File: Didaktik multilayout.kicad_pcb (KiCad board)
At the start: 2 copper layers, 212.7 x 79.4 mm, 121 parts, among them J1 Conn_01x04_MountingPin, J2 AVR-ISP-6, SW1 SW_Push_45deg, SW10 SW_Push_45deg, SW11 SW_Push_45deg, SW12 SW_Push_45deg, SW13 SW_Push_45deg, SW14 SW_Push_45deg, SW15 SW_Push_45deg, SW16 SW_Push_45deg, SW17 SW_Push_45deg, SW18 SW_Push_45deg, SW19 SW_Push_45deg, SW2 SW_Push_45deg, SW20 SW_Push_45deg, SW21 SW_Push_45deg, SW22 SW_Push_45deg, SW23 SW_Push_45deg, SW24 SW_Push_45deg, SW25 SW_Push_45deg, SW26 SW_Push_45deg, SW27 SW_Push_45deg, SW28 SW_Push_45deg, SW29 SW_Push_45deg, SW3 SW_Push_45deg, SW30 SW_Push_45deg, SW31 SW_Push_45deg, SW31a1 SW_Push_45deg, SW32 SW_Push_45deg, SW32a1 SW_Push_45deg, SW33 SW_Push_45deg, SW33a1 SW_Push_45deg, SW34 SW_Push_45deg, SW34a1 SW_Push_45deg, SW34b1 SW_Push_45deg, SW35 SW_Push_45deg, SW35a1 SW_Push_45deg, SW35b1 SW_Push_45deg, SW35c1 SW_Push_45deg, SW36 SW_Push_45deg, SW36a1 SW_Push_45deg, SW36b1 SW_Push_45deg, SW36c1 SW_Push_45deg, SW37 SW_Push_45deg, SW37a1 SW_Push_45deg, SW37b1 SW_Push_45deg, SW38 SW_Push_45deg, SW38a1 SW_Push_45deg, SW39 SW_Push_45deg, SW39a1 SW_Push_45deg, SW4 SW_Push_45deg, SW40 SW_Push_45deg, SW40a1 SW_Push_45deg, SW5 SW_Push_45deg, SW6 SW_Push_45deg, SW7 SW_Push_45deg, SW8 SW_Push_45deg, SW9 SW_Push_45deg, U1 ATmega32U4-M, Y1 Crystal_GND24_Small

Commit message: redoing placement, first routing line tests
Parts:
- moved D32 6.55 mm to (196.8, 79.4)
- moved D36 6.55 mm to (215.9, 79.4)
- moved D40 6.55 mm to (234.9, 79.4)
- moved D23 6.35 mm to (158.8, 81.0)
- moved D28 6.35 mm to (177.8, 81.0)
- moved D15 6.35 mm to (120.7, 81.0)
- moved D3 6.35 mm to (63.5, 81.0)
- moved D11 6.35 mm to (101.6, 81.0)
- moved D19 6.35 mm to (139.7, 81.0)
- moved D7 6.35 mm to (82.5, 81.0)
- moved D16 3.55 mm to (101.6, 101.6)
- moved D12 3.18 mm to (76.2, 101.6)
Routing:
- net ROW2: track 0.00 -> 58.4 mm
- net ROW3: track 0.00 -> 25.4 mm
- net Net-(D12-Pad2): track 0.00 -> 7.11 mm
- net Net-(D36-Pad2): track 0.00 -> 3.69 mm
- net Net-(D32-Pad2): track 0.00 -> 3.69 mm
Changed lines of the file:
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@@
   )
   (footprint "Diode_SMD:D_SOD-123" (layer "B.Cu")
-    (at 228.6 80.9625 90)
+    (at 234.95 79.375 90)
     (descr "SOD-123")
     (tags "SOD-123")
@@
   )
   (footprint "Diode_SMD:D_SOD-123" (layer "B.Cu")
-    (at 57.15 80.9625 90)
+    (at 63.5 80.9625 90)
     (descr "SOD-123")
     (tags "SOD-123")
@@
   )
   (footprint "Diode_SMD:D_SOD-123" (layer "B.Cu")
-    (at 209.55 80.9625 90)
+    (at 215.9 79.375 90)
     (descr "SOD-123")
     (tags "SOD-123")
@@
   )
   (footprint "Diode_SMD:D_SOD-123" (layer "B.Cu")
-    (at 190.5 80.9625 90)
+    (at 196.85 79.375 90)
     (descr "SOD-123")
     (tags "SOD-123")
@@
   )
   (footprint "Diode_SMD:D_SOD-123" (layer "B.Cu")
-    (at 114.3 80.9625 90)
+    (at 120.65 80.9625 90)
     (descr "SOD-123")
     (tags "SOD-123")
@@
   )
   (footprint "Diode_SMD:D_SOD-123" (layer "B.Cu")
-    (at 152.4 80.9625 90)
+    (at 158.75 81.025 90)
     (descr "SOD-123")
     (tags "SOD-123")
@@
   )
   (footprint "Diode_SMD:D_SOD-123" (layer "B.Cu")
-    (at 76.2 80.9625 90)
+    (at 82.55 80.9625 90)
     (descr "SOD-123")
     (tags "SOD-123")
@@
   )
   (footprint "Diode_SMD:D_SOD-123" (layer "B.Cu")
-    (at 76.2 104.775 90)
+    (at 76.2 101.6 90)
     (descr "SOD-123")
     (tags "SOD-123")
@@
   )
   (footprint "Diode_SMD:D_SOD-123" (layer "B.Cu")
-    (at 100.0125 104.775 90)
+    (at 101.6 101.6 90)
     (descr "SOD-123")
     (tags "SOD-123")
@@
   )
   (footprint "Diode_SMD:D_SOD-123" (layer "B.Cu")
-    (at 171.45 80.9625 90)
+    (at 177.8 80.9625 90)
     (descr "SOD-123")
     (tags "SOD-123")
@@
   )
   (footprint "Diode_SMD:D_SOD-123" (layer "B.Cu")
-    (at 133.35 80.9625 90)
+    (at 139.7 80.9625 90)
     (descr "SOD-123")
     (tags "SOD-123")
@@
   )
   (footprint "Diode_SMD:D_SOD-123" (layer "B.Cu")
-    (at 95.25 80.9625 90)
+    (at 101.6 80.9625 90)
     (descr "SOD-123")
     (tags "SOD-123")
@@
     (effects (font (size 1 1) (thickness 0.15)) (justify mirror))
   )
+  (segment (start 91.44 93.345) (end 91.44 100.457) (width 0.25) (layer "B.Cu") (net 12))
+  (segment (start 196.215 74.295) (end 196.85 74.93) (width 0.25) (layer "B.Cu") (net 29))
+  (segment (start 196.85 74.93) (end 196.85 77.725) (width 0.25) (layer "B.Cu") (net 29))
+  (segment (start 215.265 74.295) (end 215.9 74.93) (width 0.25) (layer "B.Cu") (net 33))
+  (segment (start 215.9 74.93) (end 215.9 77.725) (width 0.25) (layer "B.Cu") (net 33))
+  (segment (start 76.2 103.25) (end 101.6 103.25) (width 0.25) (layer "B.Cu") (net 72))
+  (segment (start 197.568901 81.743901) (end 215.181099 81.743901) (width 0.25) (layer "B.Cu") (net 73))
+  (segment (start 234.231099 81.743901) (end 234.95 81.025) (width 0.25) (layer "B.Cu") (net 73))
+  (segment (start 215.9 81.025) (end 216.618901 81.743901) (width 0.25) (layer "B.Cu") (net 73))
+  (segment (start 216.618901 81.743901) (end 234.231099 81.743901) (width 0.25) (layer "B.Cu") (net 73))
+  (segment (start 158.75 82.675) (end 177.7375 82.675) (width 0.25) (layer "B.Cu") (net 73))
+  (segment (start 215.181099 81.743901) (end 215.9 81.025) (width 0.25) (layer "B.Cu") (net 73))
+  (segment (start 196.85 81.025) (end 197.568901 81.743901) (width 0.25) (layer "B.Cu") (net 73))
+  (segment (start 177.7375 82.675) (end 177.8 82.6125) (width 0.25) (layer "B.Cu") (net 73))
   (zone (net 0) (net_name "") (layers F&B.Cu) (hatch edge 0.508)
     (connect_pads (clearance 0))

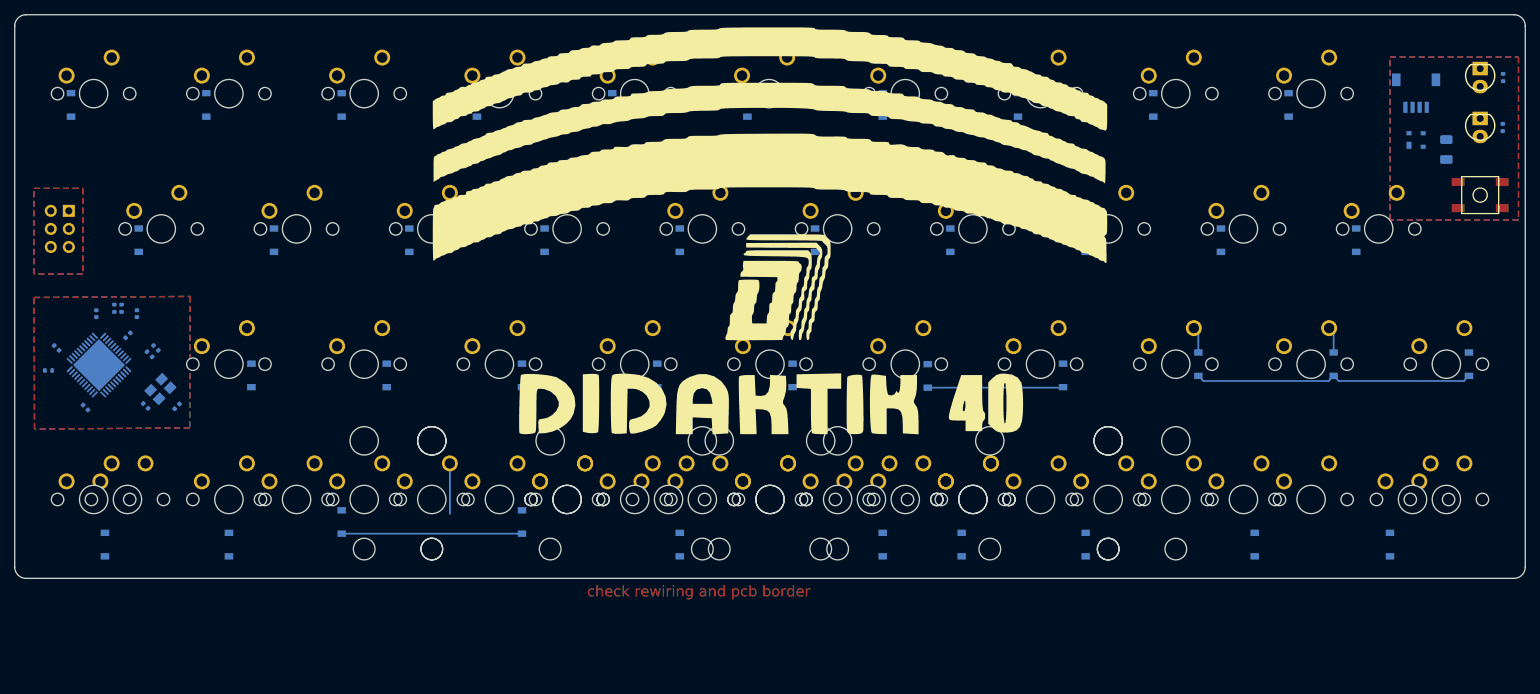
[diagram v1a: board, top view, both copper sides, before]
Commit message: revision multilayout
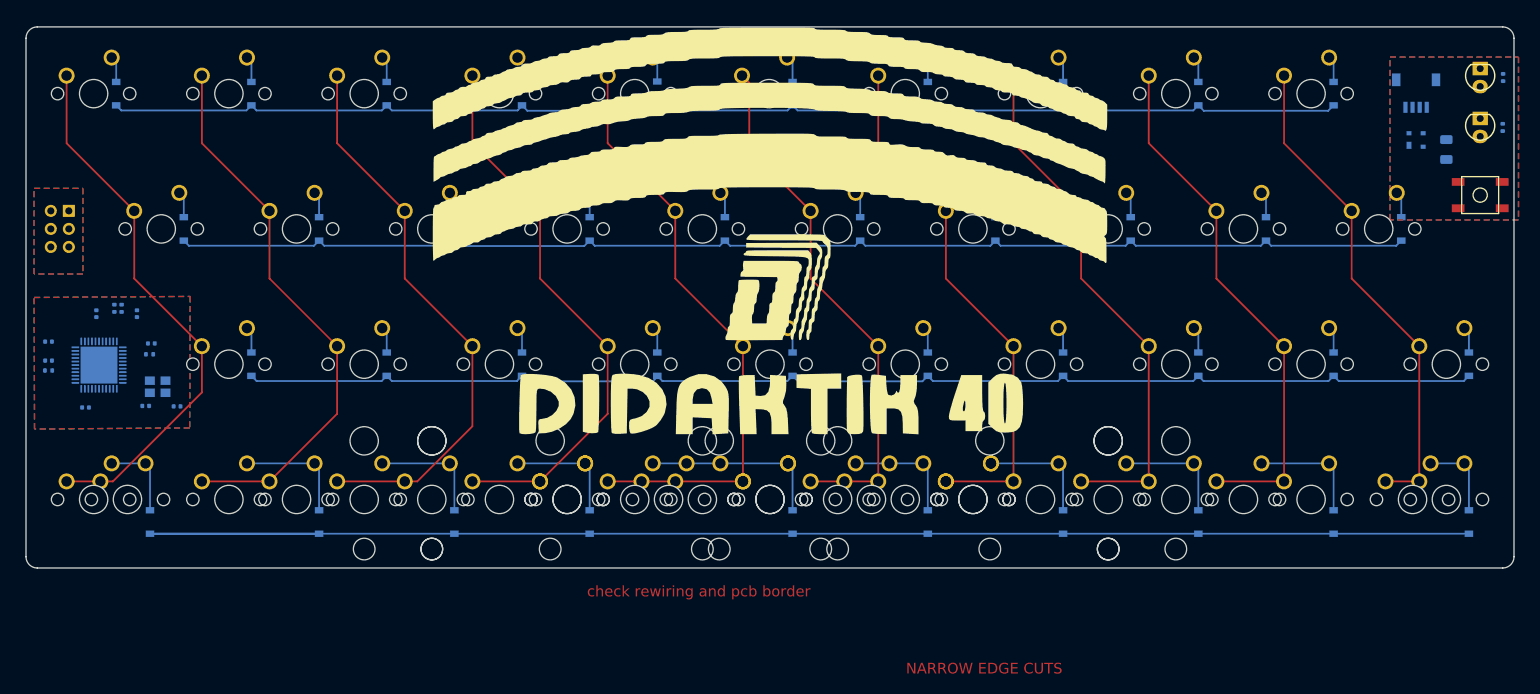
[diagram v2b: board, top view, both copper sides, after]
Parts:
- moved D33 16.2 mm to (196.8, 101.6)
- moved D20 16.2 mm to (139.7, 101.6)
- moved D12 15.9 mm to (92.1, 101.6)
- moved D29 14.6 mm to (177.8, 101.6)
- moved D8 13.1 mm to (73.0, 101.6)
- moved C6 11.7 mm to (34.9, 78.9), turned to 0 degrees
- moved D37 11.6 mm to (215.9, 101.6)
- moved D41 11.6 mm to (234.9, 101.6)
- moved D16 9.53 mm to (111.1, 101.6)
- moved D4 7.10 mm to (49.2, 101.6)
- moved D24 7.10 mm to (158.8, 101.6)
- moved D17 6.56 mm to (120.7, 41.2)
- moved D30 6.55 mm to (177.8, 41.3)
- moved D39 6.55 mm to (225.4, 60.3)
- moved D10 6.55 mm to (92.1, 60.3)
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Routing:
- net ROW3: track 25.4 -> 209.5 mm
- net ROW0: track 0.00 -> 177.0 mm
- net ROW1: track 0.00 -> 176.8 mm
- net ROW2: track 58.4 -> 177.0 mm
- net COL4: track 0.00 -> 84.1 mm
- net COL2: track 0.00 -> 79.5 mm
- net COL3: track 0.00 -> 78.5 mm
- net COL1: track 0.00 -> 78.5 mm
- net COL0: track 0.00 -> 76.8 mm
- net COL5: track 0.00 -> 74.6 mm
- net COL7: track 0.00 -> 74.6 mm
- net COL6: track 0.00 -> 74.6 mm
- net COL8: track 0.00 -> 74.6 mm
- net COL9: track 0.00 -> 69.8 mm
- net Net-(D20-Pad2): track 0.00 -> 25.9 mm
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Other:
- board size 212.7 x 79.4 mm -> 209.6 x 76.2 mm
- board text added: "NARROW EDGE CUTS"

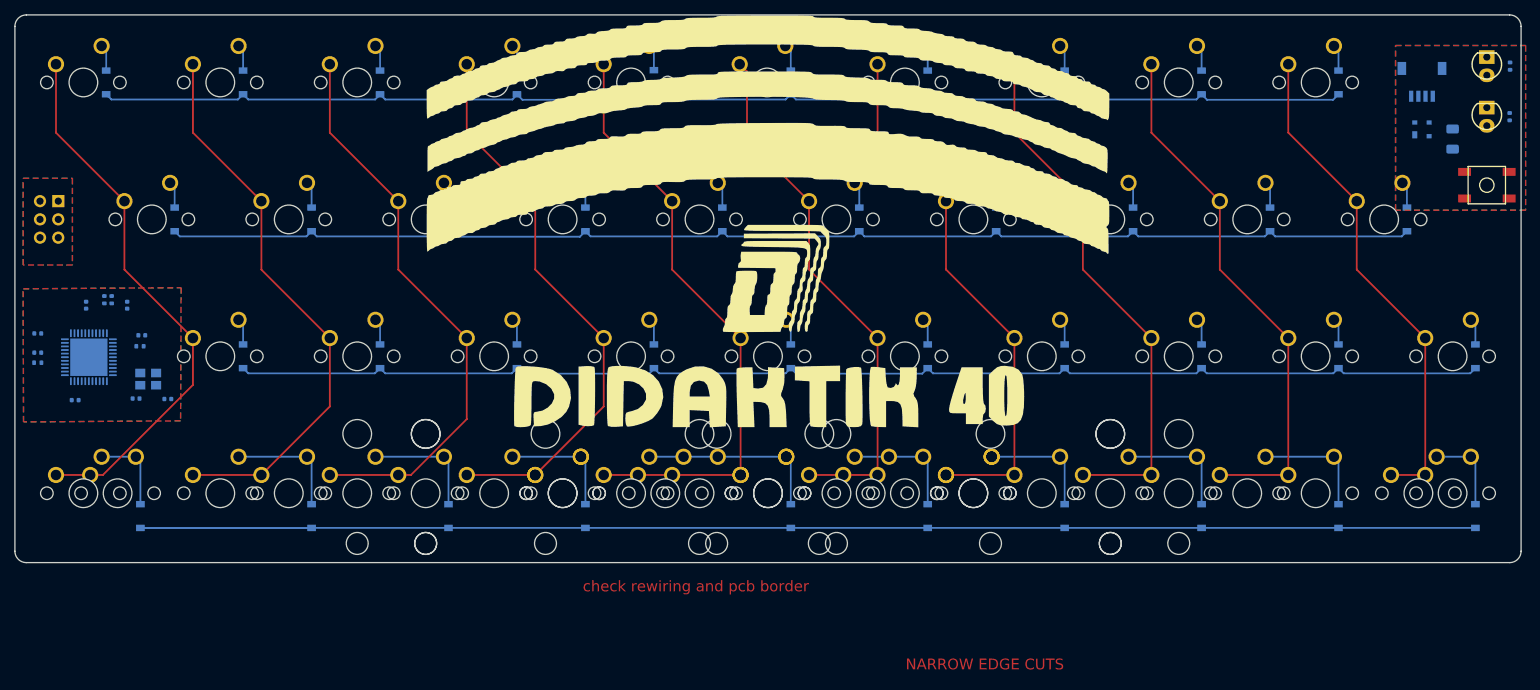
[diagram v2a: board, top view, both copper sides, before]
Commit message: reworking mcu placement and wiring
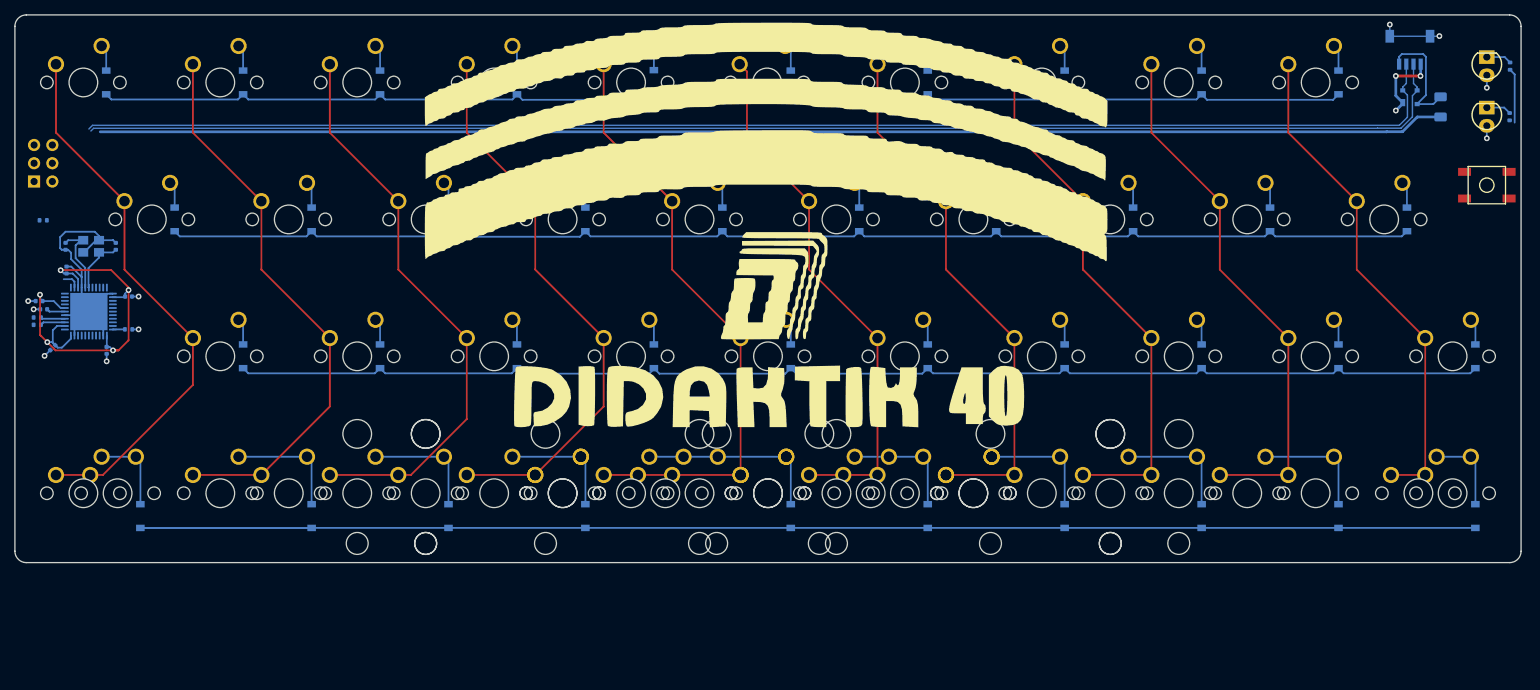
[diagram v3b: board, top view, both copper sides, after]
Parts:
- moved C4 25.6 mm to (38.8, 64.1), turned to 90 degrees
- moved R3 22.1 mm to (35.7, 60.5)
- moved C3 21.4 mm to (45.8, 64.1), turned to -90 degrees
- moved Y1 20.1 mm to (42.4, 64.1), turned to 180 degrees
- moved C5 13.6 mm to (47.6, 71.1)
- moved R4 13.5 mm to (47.6, 75.6), turned to 0 degrees
- moved C8 12.3 mm to (35.1, 71.7), turned to 180 degrees
- moved R2 10.6 mm to (34.9, 74.0), turned to 0 degrees
- moved R1 9.97 mm to (34.9, 75.0), turned to 0 degrees
- moved C2 7.94 mm to (37.0, 78.2), turned to -135 degrees
- moved J2 7.85 mm to (35.7, 52.5), turned to 180 degrees
- moved U1 6.35 mm to (42.0, 73.2)
- moved C6 6.09 mm to (35.8, 72.8), turned to 180 degrees
- moved C1 5.60 mm to (38.9, 67.4)
- moved C7 5.32 mm to (44.5, 78.5), turned to -90 degrees
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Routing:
- net +5V: track 0.00 -> 248.2 mm, vias 0 -> 5
- net D+: track 0.00 -> 192.5 mm
- net D-: track 0.00 -> 192.0 mm
- net GND: track 0.00 -> 63.6 mm, vias 0 -> 11
- net VCC: track 0.00 -> 15.8 mm
- net XTAL2: track 0.00 -> 10.4 mm
- net (no net): track 0.00 -> 8.54 mm, vias 0 -> 2
- net XTAL1: track 0.00 -> 8.02 mm
- net LED capslock: track 0.00 -> 7.62 mm
- net Net-(D43-Pad2): track 0.00 -> 3.54 mm
- net Net-(D42-Pad2): track 0.00 -> 3.49 mm
- net Net-(R1-Pad2): track 0.00 -> 3.47 mm
- net Net-(R2-Pad2): track 0.00 -> 3.40 mm
- net Net-(C6-Pad1): track 0.00 -> 2.60 mm
- net RESET: track 0.00 -> 2.46 mm
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- removed copper zone on B.Cu, net (none)
- removed copper zone on F.Cu, net (none)
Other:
- board text removed: "NARROW EDGE CUTS"
- board text removed: "check rewiring and pcb border"

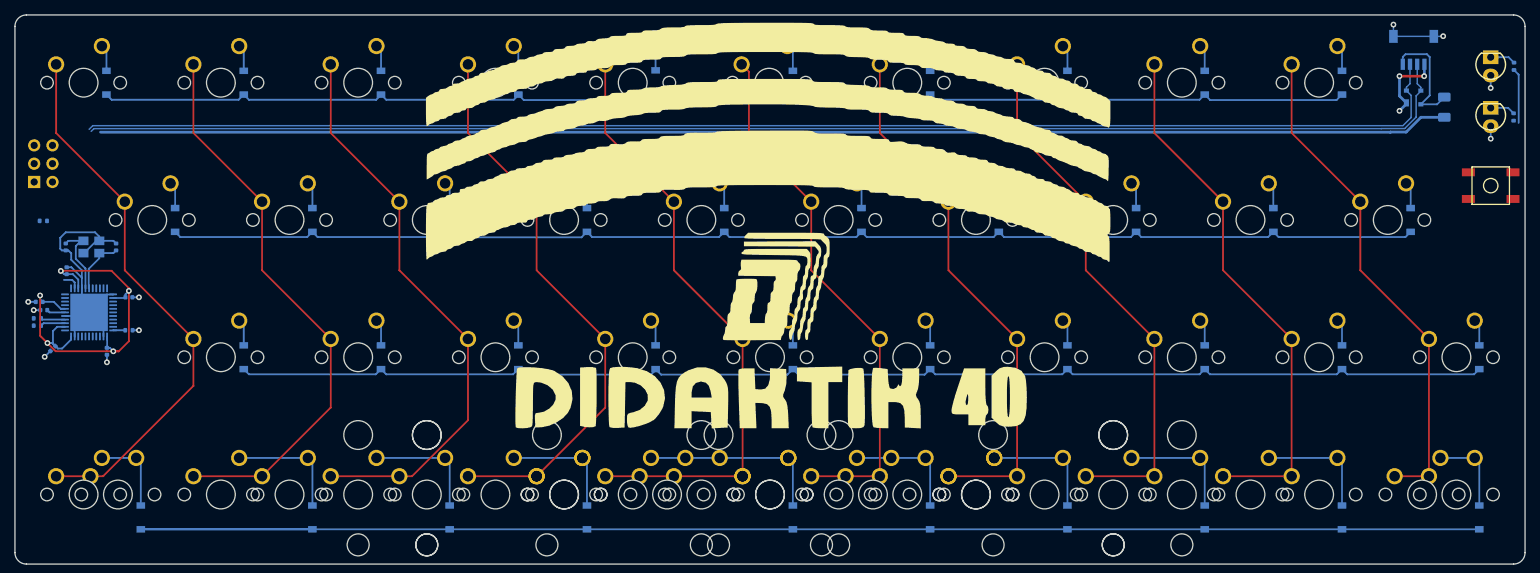
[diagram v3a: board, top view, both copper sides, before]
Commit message: full routing of mcu & matrix
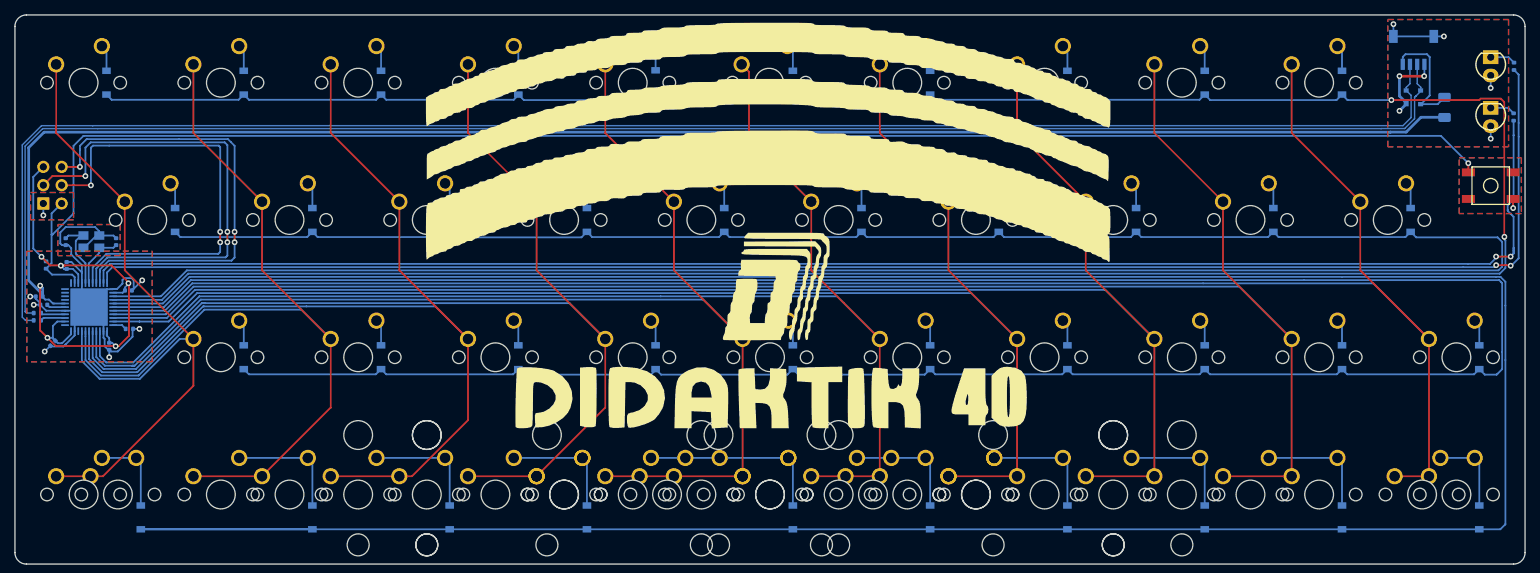
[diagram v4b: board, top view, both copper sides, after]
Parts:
- moved R3 6.14 mm to (36.1, 66.6), turned to -90 degrees
- moved J2 3.24 mm to (37.0, 55.5)
- moved C5 0.95 mm to (47.5, 70.1)
- moved C7 0.77 mm to (44.8, 77.9)
- moved C1 0.73 mm to (38.9, 66.6)
- moved C3 0.73 mm to (45.8, 63.3)
- moved C4 0.73 mm to (38.8, 63.3)
- moved C6 0.73 mm to (35.8, 72.1)
- moved C8 0.73 mm to (35.1, 71.0)
- moved R1 0.73 mm to (34.9, 74.3)
- moved R2 0.73 mm to (34.9, 73.2)
- moved U1 0.73 mm to (42.0, 72.4)
- moved Y1 0.73 mm to (42.4, 63.3)
- moved C2 0.73 mm to (37.0, 77.4)
- moved R4 0.20 mm to (47.6, 75.4)
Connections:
- U1 pad 10: LED Power -> unconnected-(U1-Pad10)
- U1 pad 11: LED capslock -> unconnected-(U1-Pad11)
- U1 pad 12: COL9 -> unconnected-(U1-Pad12)
- U1 pad 18: unconnected-(U1-Pad18) -> SCK
- U1 pad 19: unconnected-(U1-Pad19) -> MOSI
- U1 pad 20: SCK -> MISO
- U1 pad 21: MISO -> LED Power
- U1 pad 22: MOSI -> LED capslock
- U1 pad 25: unconnected-(U1-Pad25) -> ROW1
- U1 pad 26: unconnected-(U1-Pad26) -> ROW0
- U1 pad 27: ROW7 -> ROW3
- U1 pad 28: COL6 -> ROW2
- U1 pad 29: COL7 -> COL9
- U1 pad 31: COL4 -> COL7
- U1 pad 32: COL5 -> COL6
- U1 pad 36: COL3 -> COL5
- U1 pad 37: COL2 -> COL4
- U1 pad 38: COL1 -> COL3
- U1 pad 39: COL0 -> COL2
- U1 pad 40: ROW1 -> COL1
- U1 pad 41: ROW0 -> COL0
- U1 pad 8: ROW3 -> unconnected-(U1-Pad8)
- U1 pad 9: ROW2 -> unconnected-(U1-Pad9)
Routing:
- net ROW0: track 177.0 -> 418.2 mm, vias 0 -> 2
- net ROW3: track 209.5 -> 442.1 mm
- net RESET: track 2.46 -> 225.8 mm, vias 0 -> 1
- net LED Power: track 0.00 -> 218.3 mm, vias 0 -> 2
- net LED capslock: track 7.62 -> 224.6 mm, vias 0 -> 2
- net ROW1: track 176.8 -> 388.0 mm
- net ROW2: track 177.0 -> 387.2 mm
- net COL9: track 69.8 -> 257.2 mm
- net COL8: track 74.6 -> 242.7 mm
- net COL7: track 74.6 -> 223.5 mm
- net COL6: track 74.6 -> 204.3 mm
- net COL5: track 74.6 -> 192.9 mm
- net COL4: track 84.1 -> 184.2 mm
- net COL3: track 78.5 -> 160.2 mm
- net MOSI: track 0.00 -> 66.8 mm, vias 0 -> 3
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- added copper zone on B.Cu, net GND
- added copper zone on F.Cu, net GND
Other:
- board text added: "ISP"

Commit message: outlining case dimensions
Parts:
- added SW1: SW_Push_45deg, MX_Only:MXOnly-1U-NoLED, F.Cu at (41.3, 22.2)
- added SW1: SW_Push_45deg, MX_Only:MXOnly-1U-NoLED, F.Cu at (41.3, -15.9)
- added SW1: SW_Push_45deg, MX_Only:MXOnly-1U-NoLED, F.Cu at (41.3, 117.5)
- added SW1: SW_Push_45deg, MX_Only:MXOnly-1U-NoLED, F.Cu at (22.2, 41.3)
- added SW1: SW_Push_45deg, MX_Only:MXOnly-1U-NoLED, F.Cu at (12.7, 41.3)
- added SW1: SW_Push_45deg, MX_Only:MXOnly-1U-NoLED, F.Cu at (260.4, 79.4)
- added SW1: SW_Push_45deg, MX_Only:MXOnly-1U-NoLED, F.Cu at (41.3, 127.0)
- added SW1: SW_Push_45deg, MX_Only:MXOnly-1U-NoLED, F.Cu at (250.8, 79.4)
- added SW1: SW_Push_45deg, MX_Only:MXOnly-1U-NoLED, F.Cu at (41.3, 3.17)

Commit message: outlined case more, deliberating routing aesthetics
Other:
- board text added: "80 kB"
- board text added: "Didaktik 40"
- board text added: "caps"
- board text added: "res"
- board text added: "~"
